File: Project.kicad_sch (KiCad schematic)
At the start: 43 parts, among them J1 Screw_Terminal_01x02, J2 Screw_Terminal_01x02, J3 Conn_01x04_Socket, Q1 BT136-500, SW1 PEC11H, SW2 PEC11H, U1 AMS1117-3.3, U2 ESP32-WROOM-32, U3 MOC3021M, U4 MCT2E, U5 MAX4466EXK

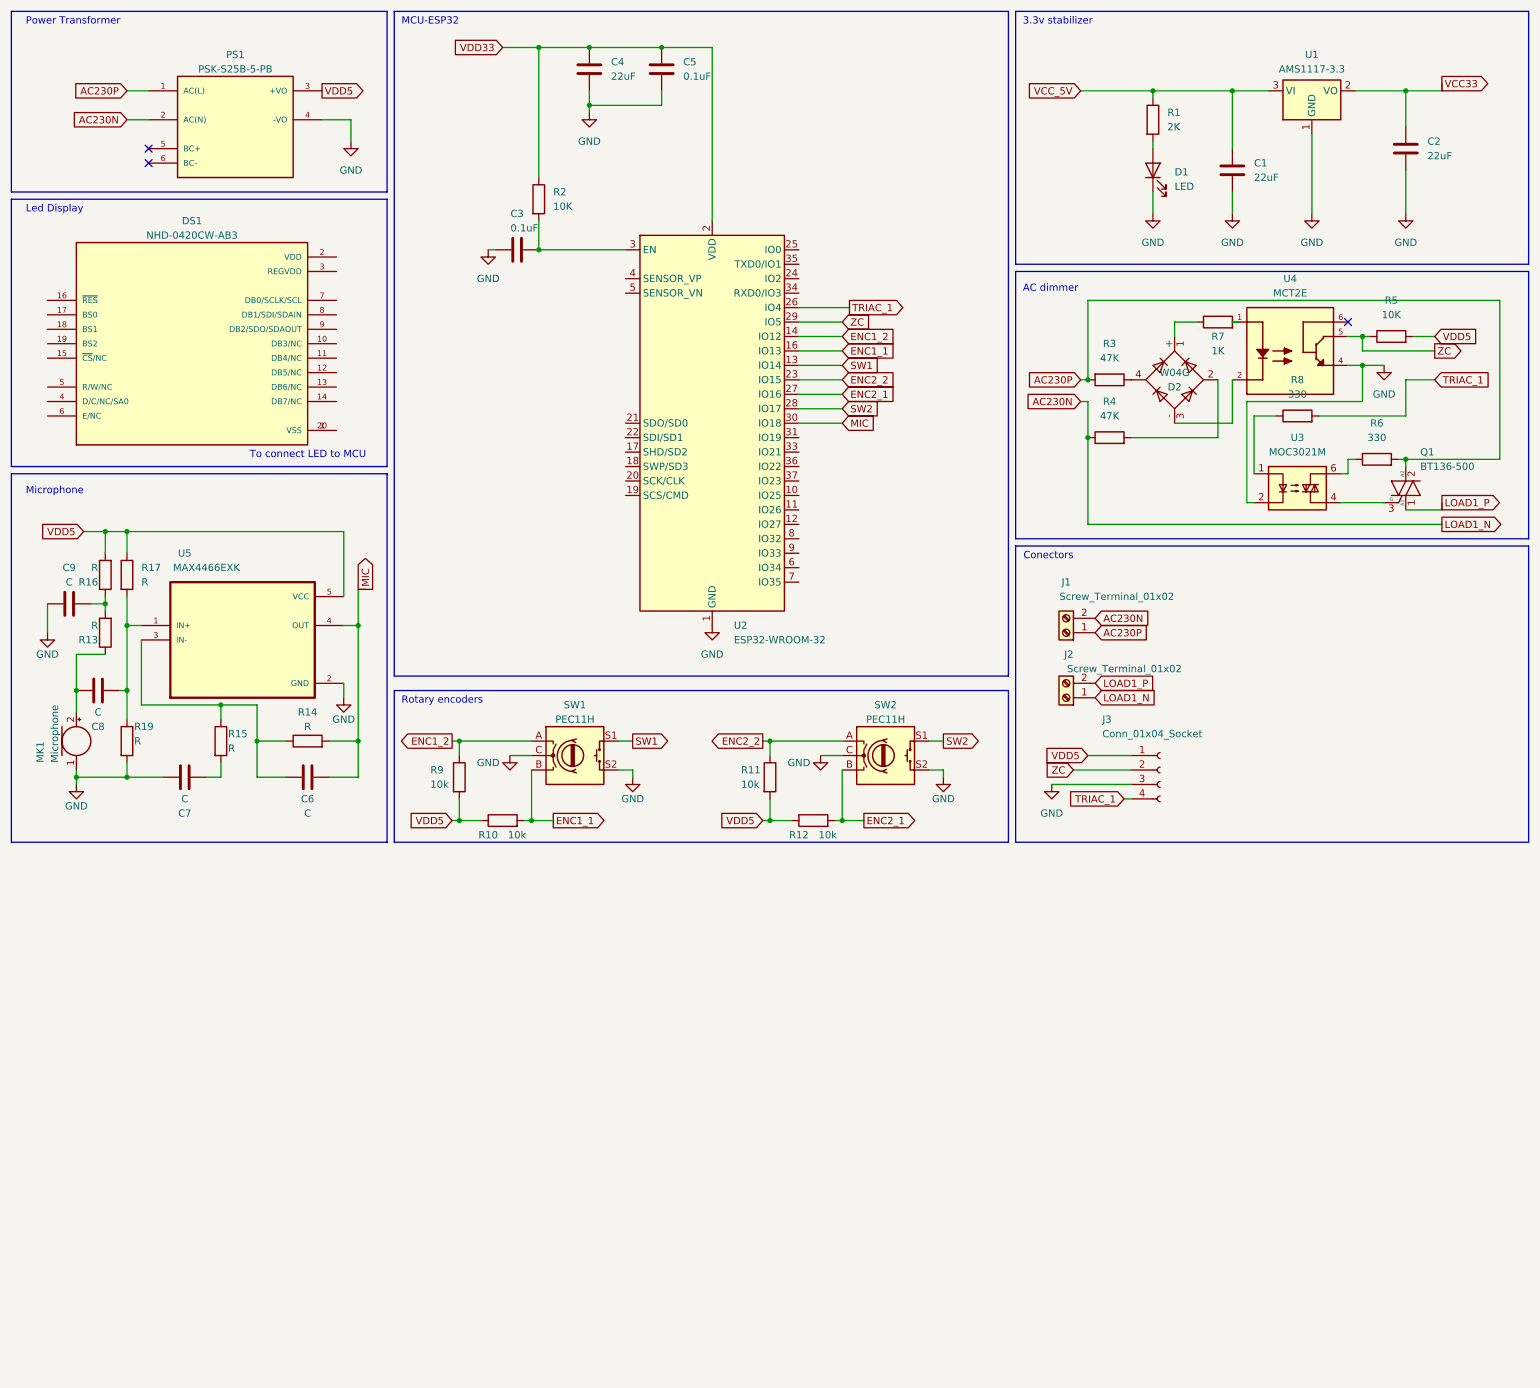
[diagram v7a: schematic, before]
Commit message: Added PIR sensor
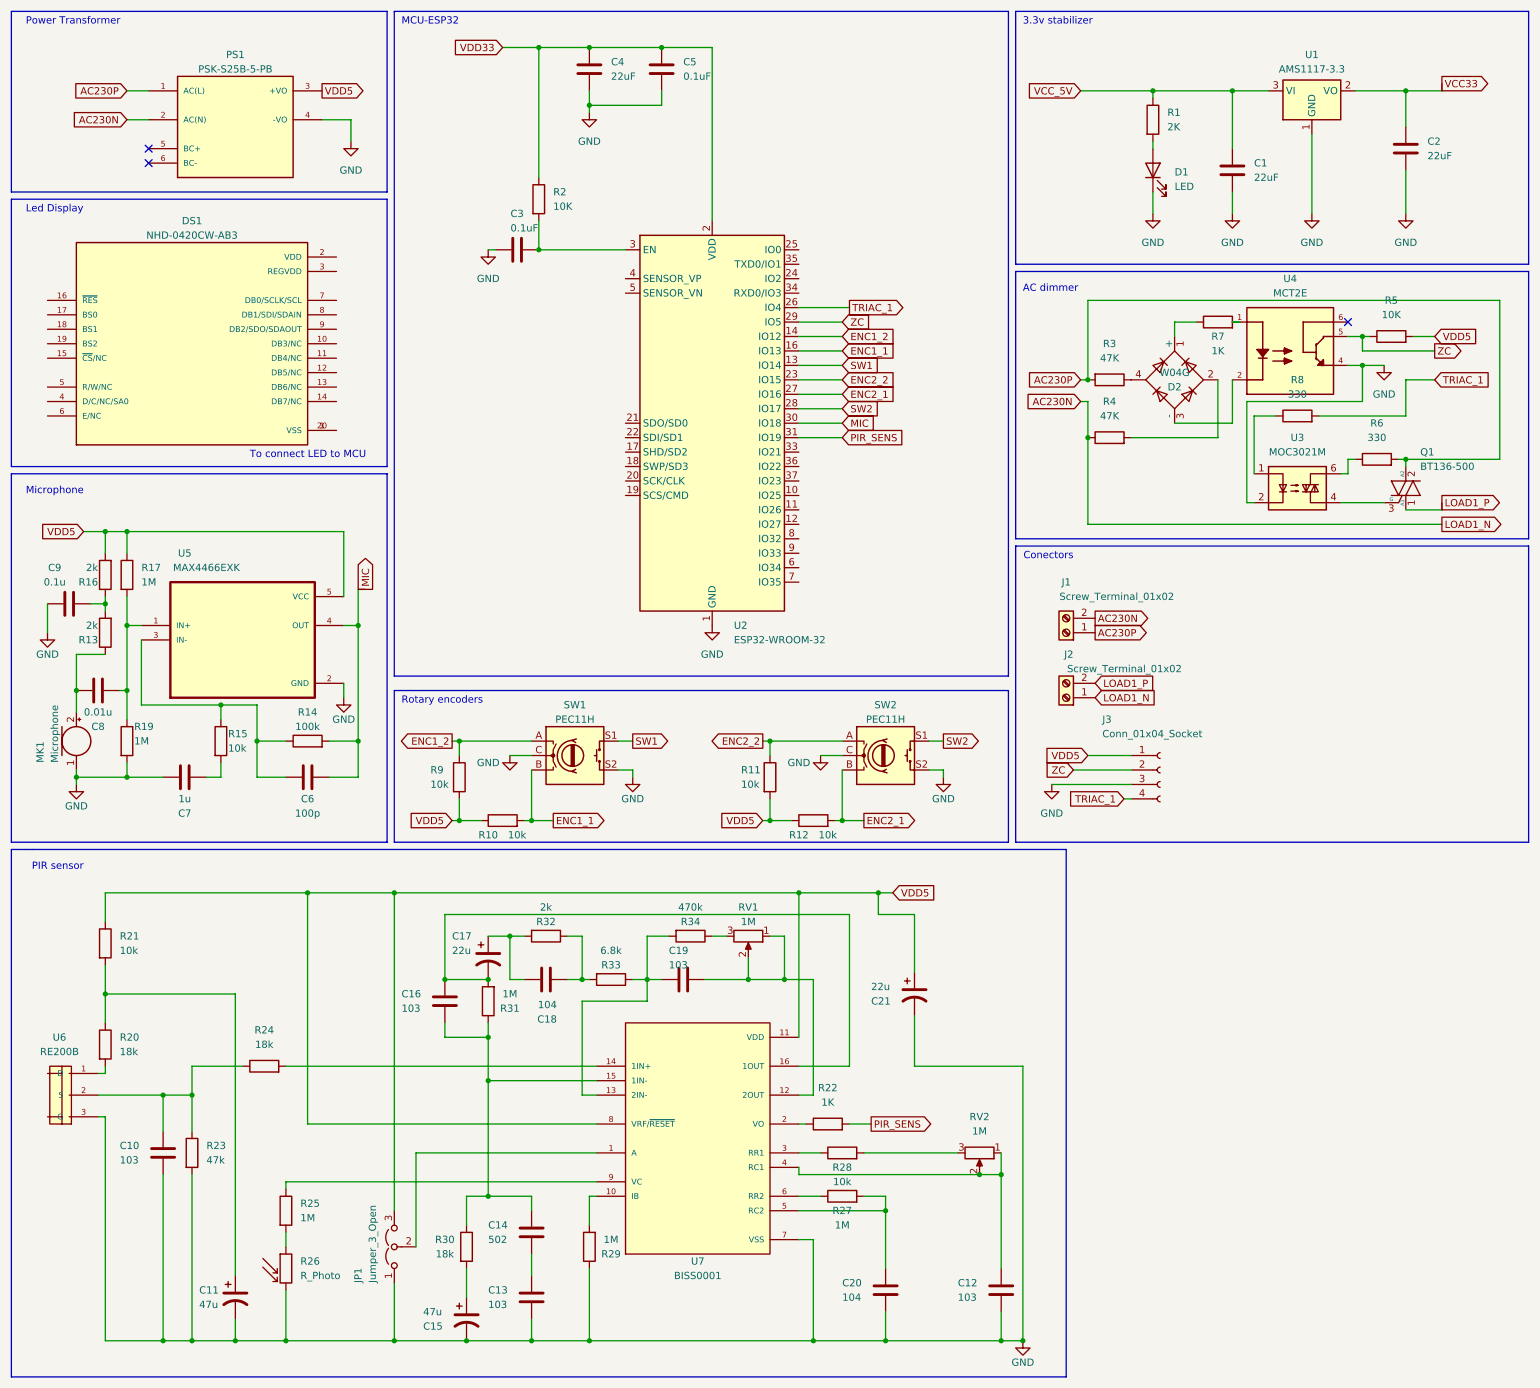
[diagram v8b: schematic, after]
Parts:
- added C10, C12, C13, C16, C19: 103, symbol Device:C
- added C11, C15: 47u, symbol Device:C_Polarized_US
- added C14: 502, symbol Device:C
- added C17, C21: 22u, symbol Device:C_Polarized_US
- added C18, C20: 104, symbol Device:C
- added JP1: Jumper_3_Open, symbol Jumper:Jumper_3_Open
- added R20, R24, R30: 18k, symbol Device:R
- added R21, R28: 10k, symbol Device:R
- added R22: 1K, symbol Device:R
- added R23: 47k, symbol Device:R
- added R25, R27, R29, R31: 1M, symbol Device:R
- added R26: R_Photo, symbol Device:R_Photo
- added R32: 2k, symbol Device:R
- added R33: 6.8k, symbol Device:R
- added R34: 470k, symbol Device:R
- added RV1, RV2: 1M, symbol Device:R_Potentiometer
- added U6: RE200B, DIP-MOTION_POSITION-LHI778_3P-D8.1MM_:SNR3-D8.1XH4.2MM, symbol DIP-MOTION_POSITION-LHI778_3P-D8.1MM:DIP-MOTION_POSITION-LHI778_3P-D8.1MM_
- added U7: BISS0001, BISS0001:SOIC127P600X180-16N, symbol BISS0001:BISS0001
- C6: value C -> 100p
- C7: value C -> 1u
- C8: value C -> 0.01u
- C9: value C -> 0.1u
- R13, R16: value R -> 2k
- R14: value R -> 100k
- R15: value R -> 10k
- R17, R19: value R -> 1M
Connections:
- net GND: now also C10.2, C11.2, C12.2, C13.2, C15.2, C20.2, C21.2, JP1.1 (A), R23.2, R26.2, R29.1, U6.3 (G), U7.7 (VSS)
- net VDD5: now also C21.1, JP1.3 (B), R21.1, U7.11 (VDD), U7.8 (VRF/~{RESET})
- net PIR_SENS: now reaches U2.31 (IO19)
- net PIR_SENS: now also R22.2
- new net: C11.1, R20.1, R21.2
- new net: C18.2, R32.1, R33.2
- new net: C17.1, C18.1, R32.2
- new net: R20.2, U6.1 (D)
- new net: C14.1, C16.2, R30.1, R31.1, U7.15 (1IN-)
- new net: C15.1, R30.2
- new net: JP1.2 (C), U7.1 (A)
- new net: C13.1, C14.2
- new net: C19.1, RV1.1, RV1.2, U7.12 (2OUT)
- new net: R34.1, RV1.3
- new net: C12.1, RV2.1, RV2.2, U7.4 (RC1)
- new net: C19.2, R33.1, R34.2, U7.13 (2IN-)
- new net: C10.1, R23.1, R24.1, U6.2 (S)
- new net: R24.2, U7.14 (1IN+)
- new net: C16.1, C17.2, R31.2, U7.16 (1OUT)
- new net: R25.2, R26.1
- new net: R29.2, U7.10 (IB)
- new net: R22.1, U7.2 (VO)
- new net: C20.1, R27.2, U7.5 (RC2)
- new net: R28.1, U7.3 (RR1)
- new net: R27.1, U7.6 (RR2)
- new net: R25.1, U7.9 (VC)
- new net: R28.2, RV2.3
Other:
- note added: "PIR sensor"
